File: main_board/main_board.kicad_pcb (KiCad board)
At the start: 4 copper layers, 85 x 55 mm, 58 parts, among them J1 USB4105-GF-A-060, J2 Conn_ARM_JTAG_SWD_10, Q3 NX3008PBK,215, U1 SSD1306, U2 ESP32-S2-SOLO, U3 TLV62568PDRLT, U4 MCP73832, U5 DW01, U6 8205A, U7 MAX17055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

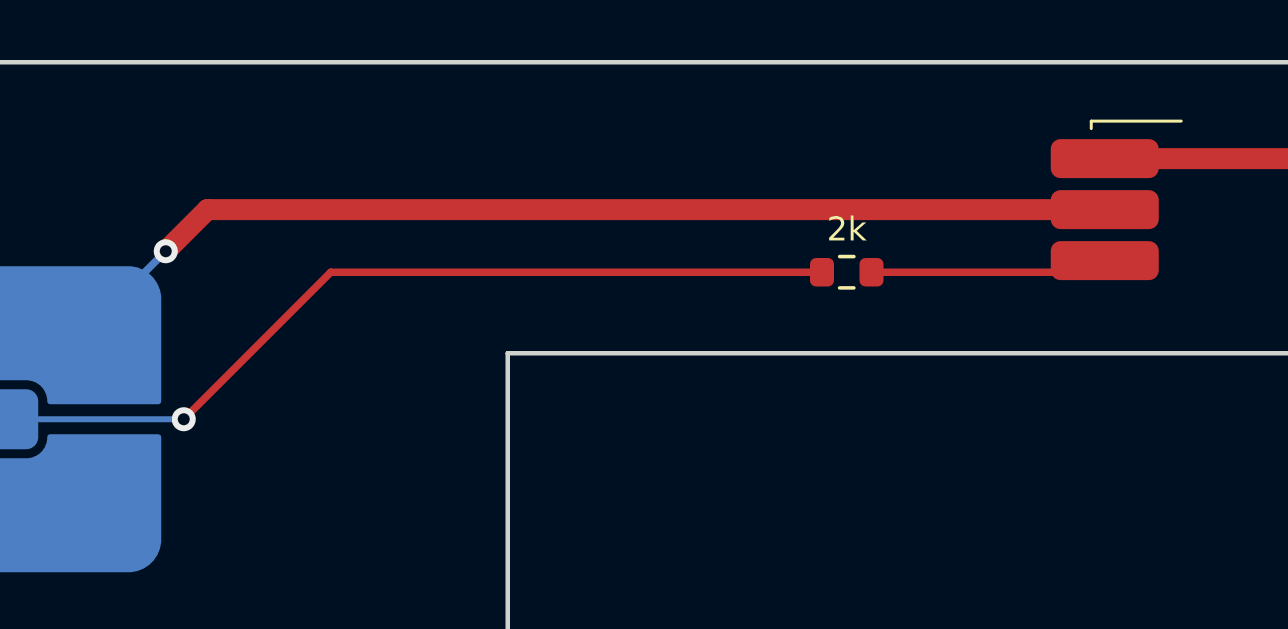
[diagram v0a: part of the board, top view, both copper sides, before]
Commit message: Tweak touch detector circuit
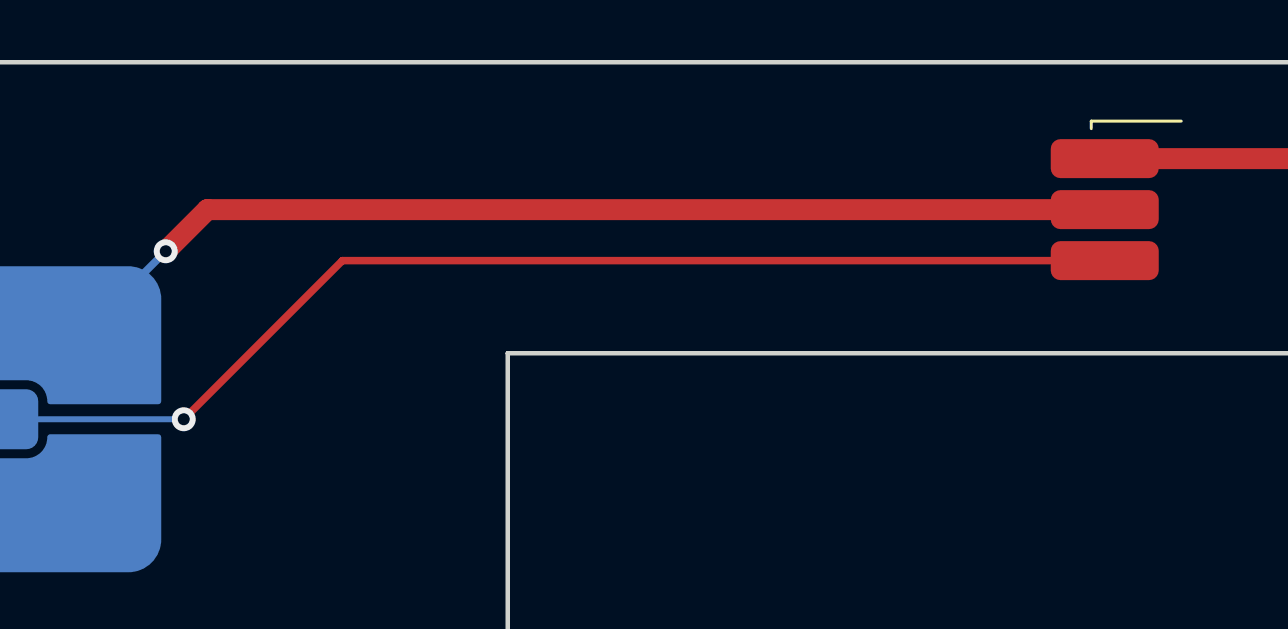
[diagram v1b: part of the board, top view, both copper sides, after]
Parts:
- removed R17: 2k, Resistor_SMD:R_0603_1608Metric
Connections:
- E2 pad 1: Net-(E2-Pad1) -> Net-(M1-RLD_OUT)
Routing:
- net Net-(M1-RLD_OUT): track 7.39 -> 38.7 mm, vias 0 -> 1
- net Net-(E2-Pad1): track 29.2 -> 0.00 mm, vias 1 -> 0

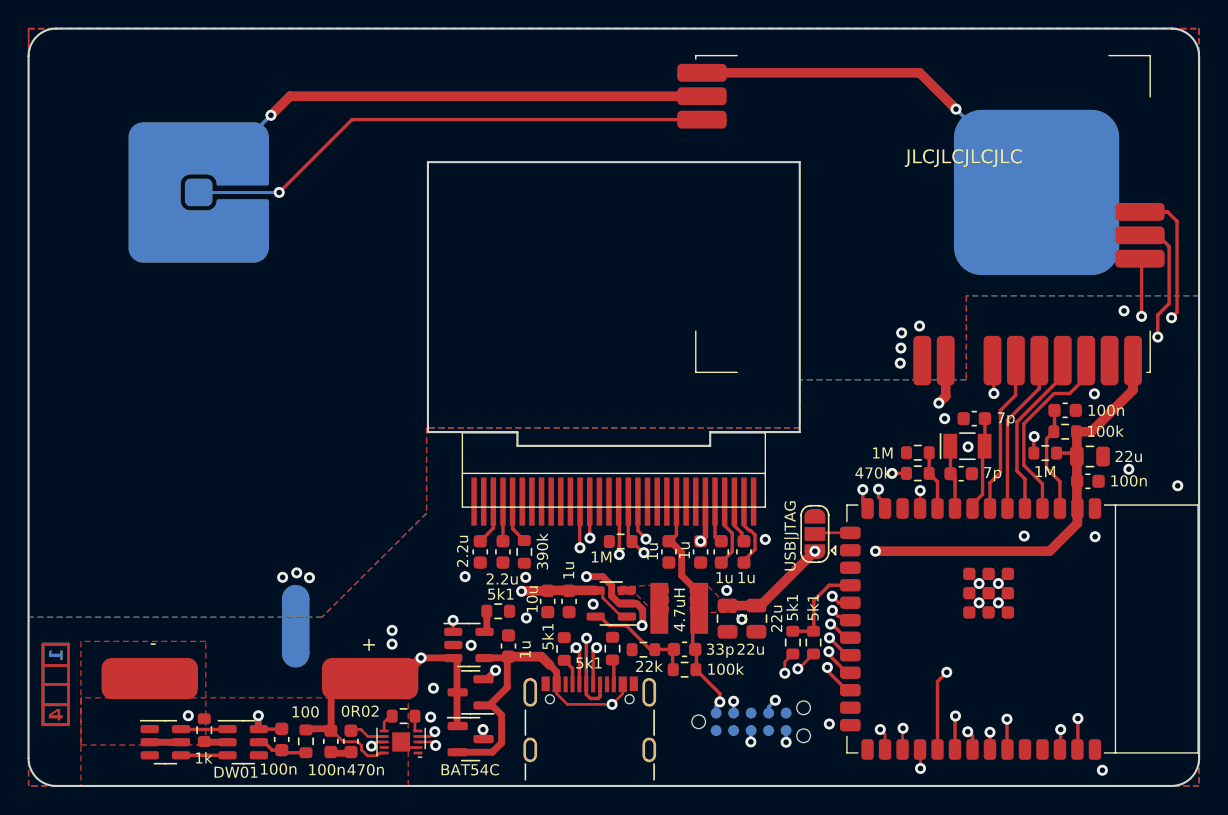
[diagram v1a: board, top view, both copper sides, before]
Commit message: Shrink frontend a bit
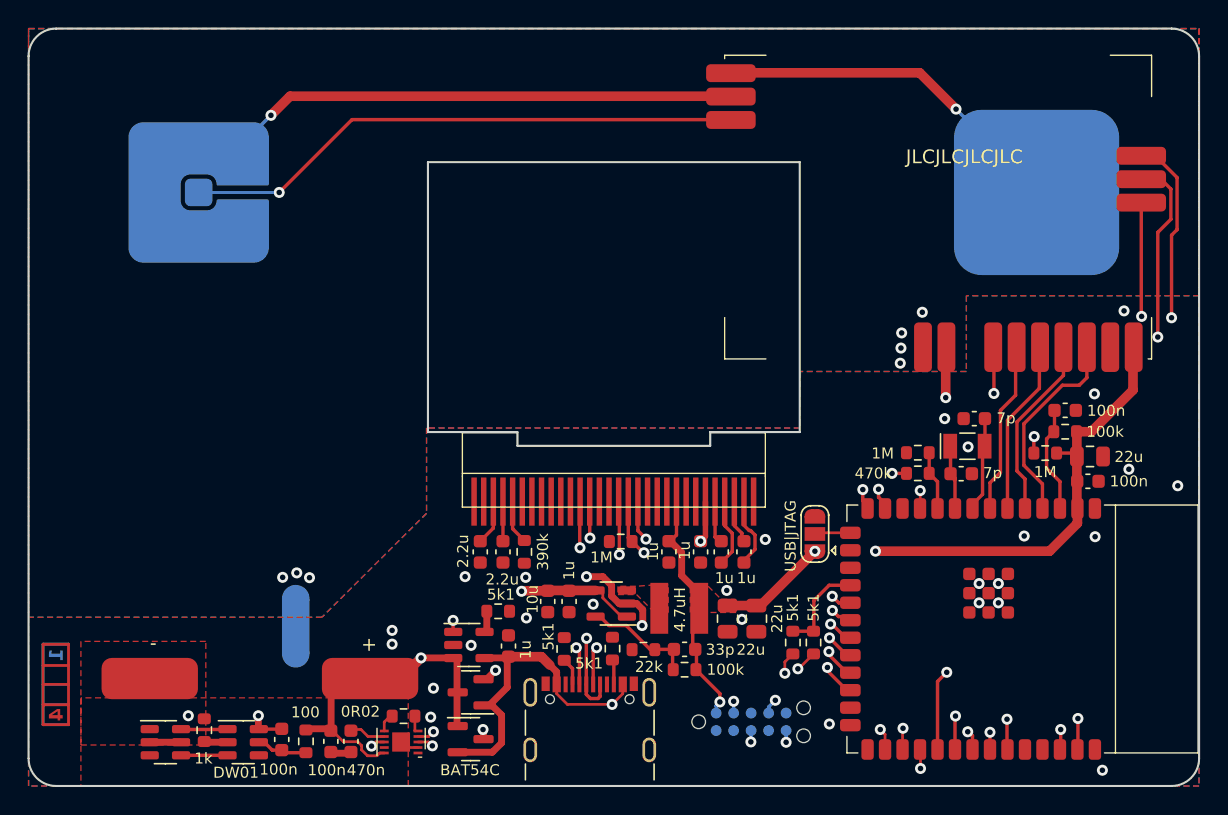
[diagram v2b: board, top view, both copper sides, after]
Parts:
- moved M1 2.32 mm to (130.8, 68.7)
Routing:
- net /ECG_CLK_EN: track 42.2 -> 46.4 mm
- net /ECG_EN: track 41.4 -> 45.5 mm
- net /~{TOUCH}: track 44.9 -> 47.4 mm
- net Net-(M1-~{DRDY}): track 13.1 -> 15.4 mm
- net Net-(M1-ECG_L): track 23.0 -> 20.9 mm
- net /BATT_SCL: track 43.3 -> 41.2 mm
- net Net-(M1-MISO): track 11.7 -> 13.9 mm
- net /BATT_SDA: track 45.5 -> 43.4 mm
- net Net-(M1-RLD_OUT): track 38.7 -> 40.8 mm
- net Net-(M1-ECG_R): track 34.7 -> 36.8 mm

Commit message: Fix rule violation, use a single plane on front side
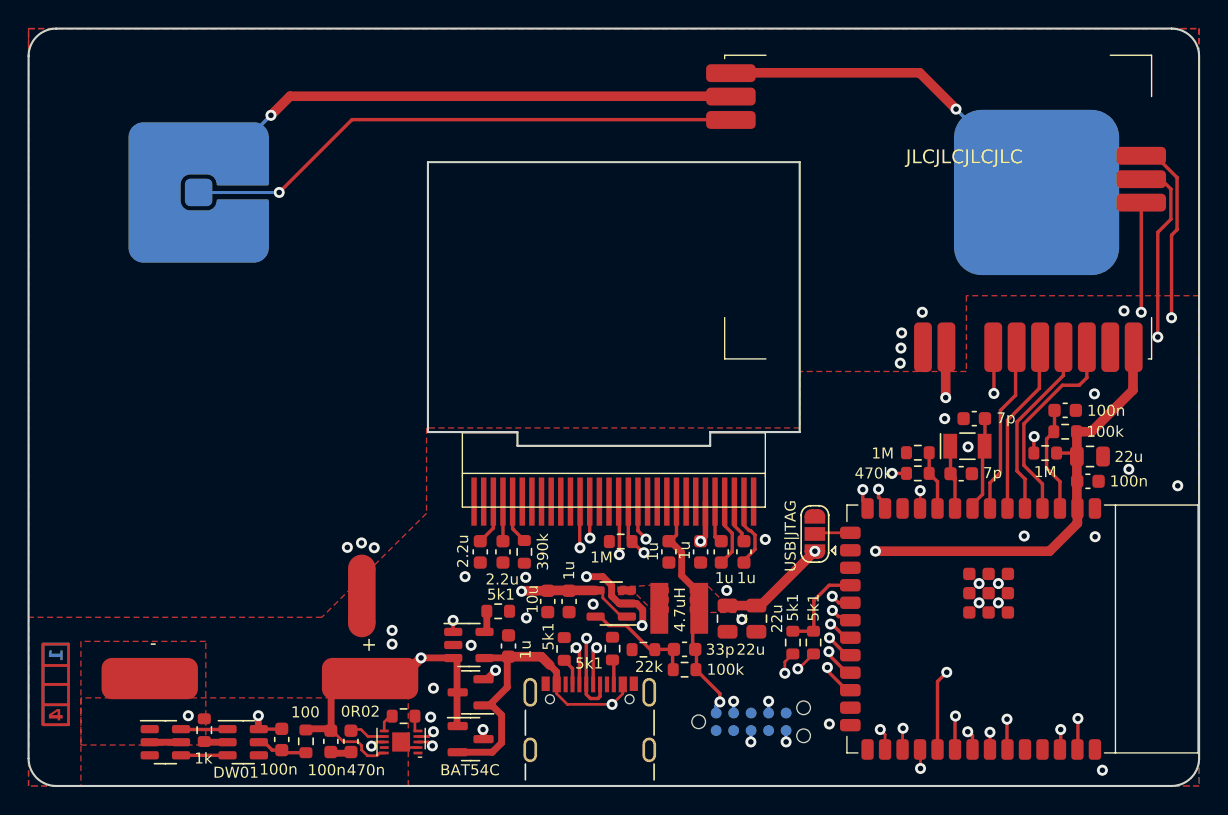
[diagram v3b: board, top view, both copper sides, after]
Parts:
- NT1: moved to F.Cu
- moved NT1 5.28 mm to (104.2, 86.2)
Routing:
- removed copper zone on B.Cu, net GNDA

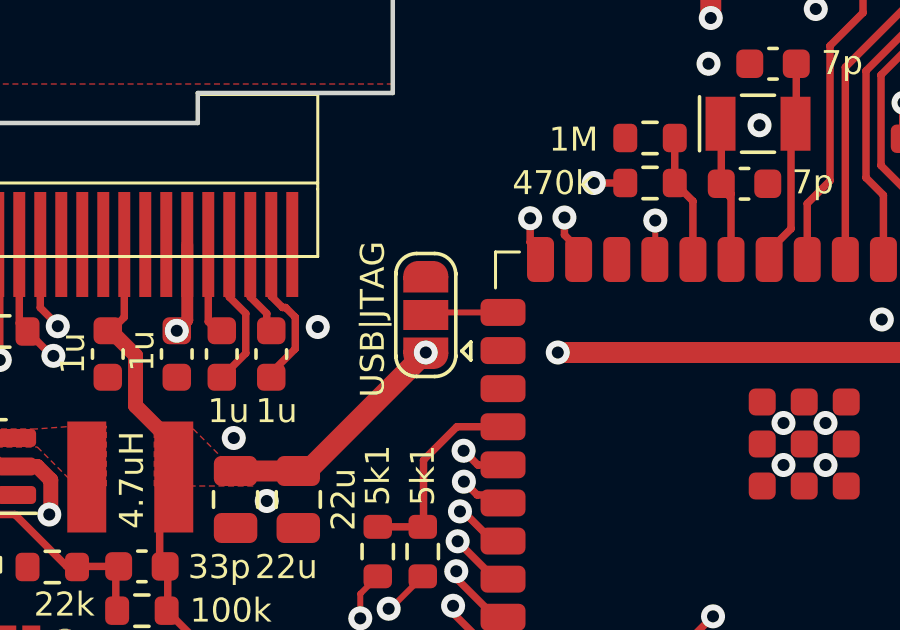
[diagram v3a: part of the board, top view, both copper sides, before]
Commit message: Remove JTAG selector
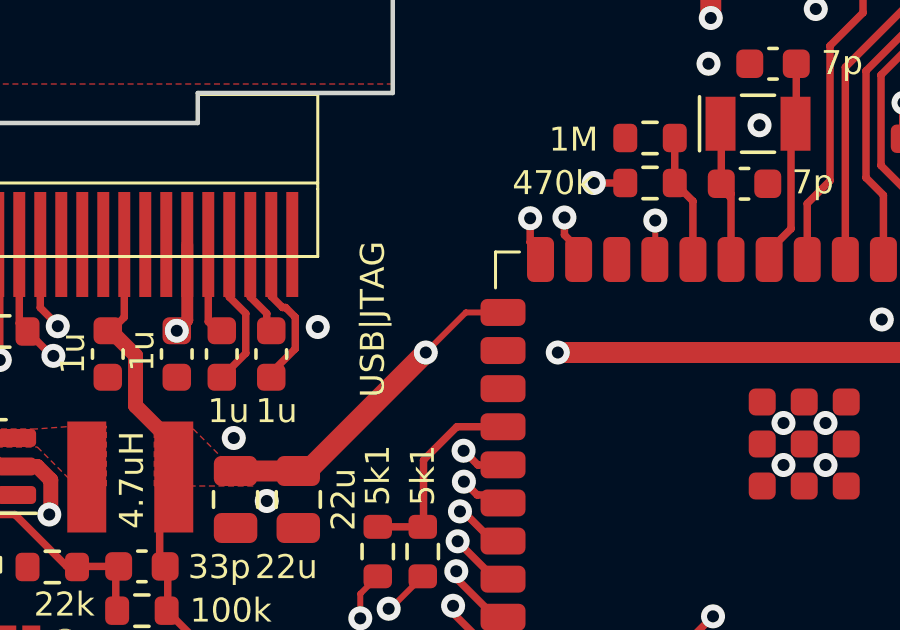
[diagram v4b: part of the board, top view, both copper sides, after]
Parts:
- removed JP1: SolderJumper_3_Open, Jumper:SolderJumper-3_P1.3mm_Open_RoundedPad1.0x1.5mm
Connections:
- U2 pad 15: Net-(JP1-C) -> +3V3
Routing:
- net +3V3: track 57.6 -> 60.8 mm
- net Net-(JP1-C): track 2.54 -> 0.00 mm

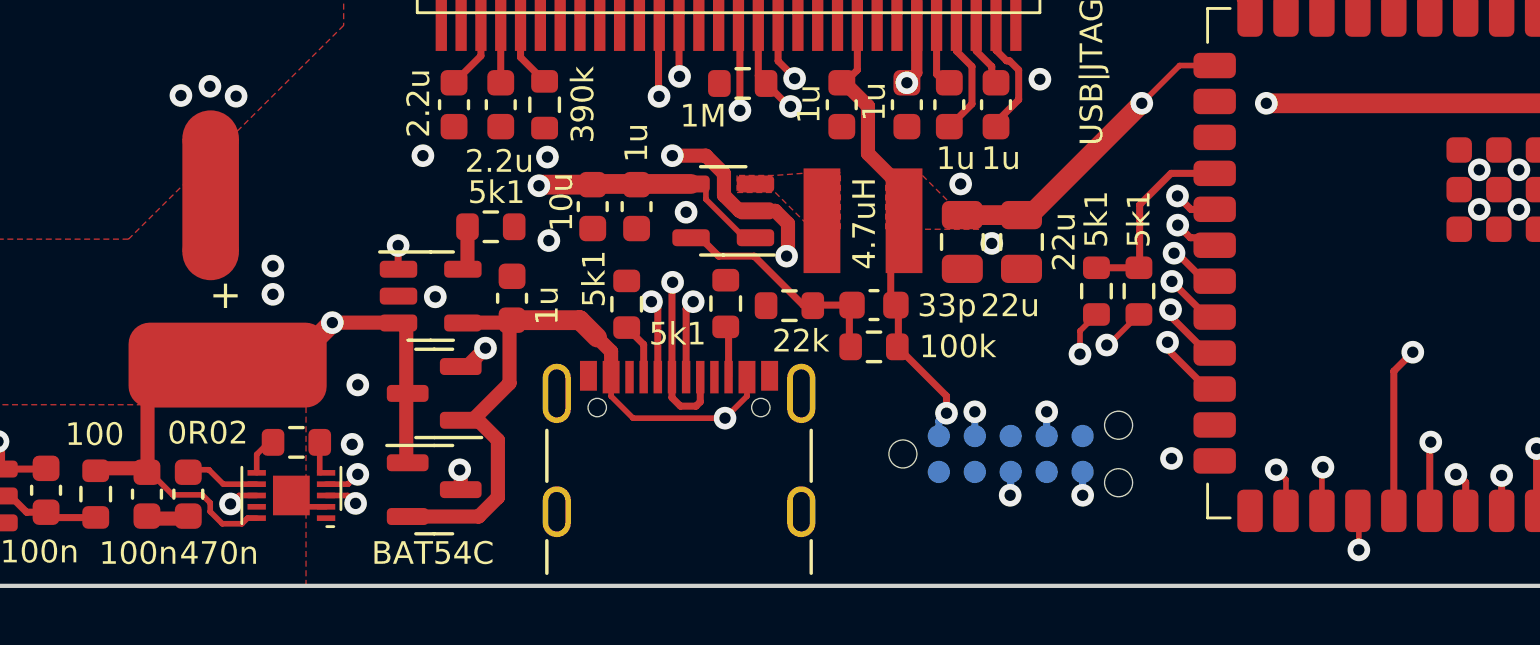
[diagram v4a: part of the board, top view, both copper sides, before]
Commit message: Replace battery alert input with ADC_EN
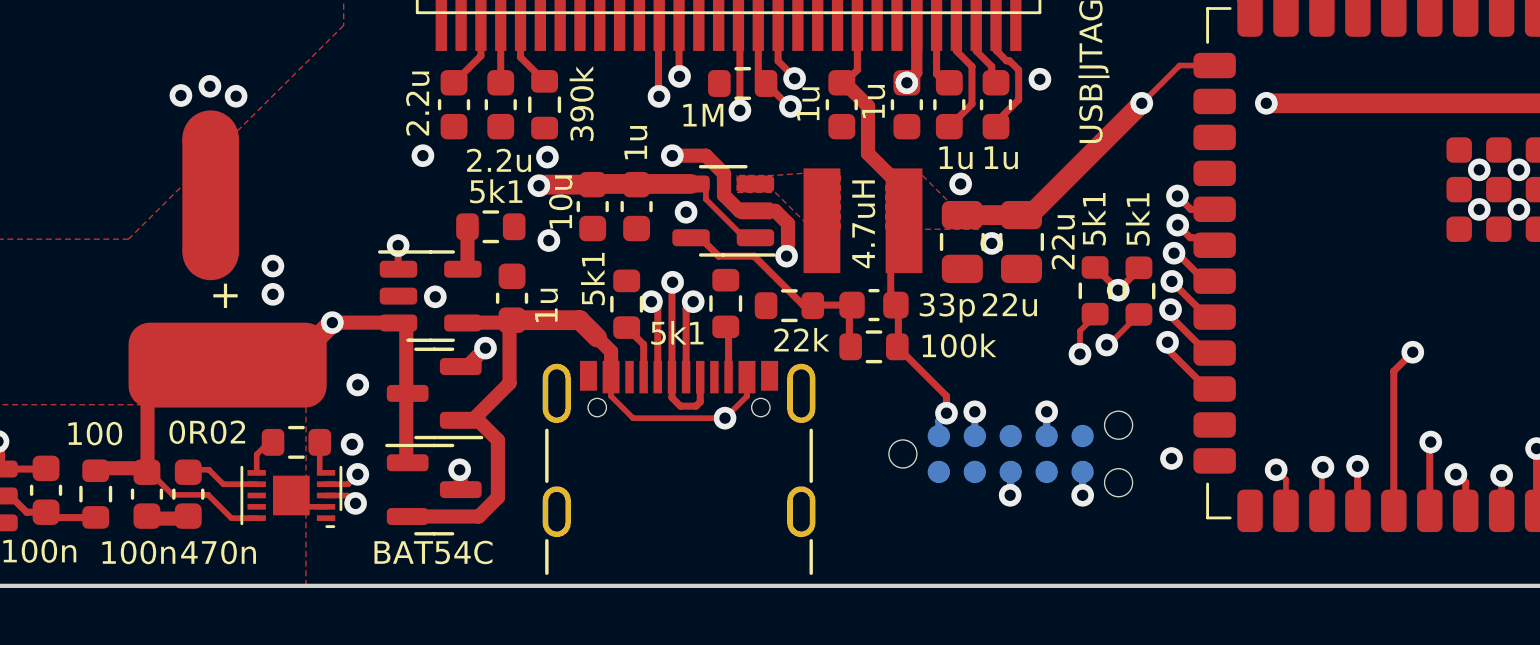
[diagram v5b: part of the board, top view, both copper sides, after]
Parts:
- moved R9 0.05 mm to (135.4, 89.6)
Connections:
- U2 pad 18: /ADC_EN -> unconnected-(U2-IO10-Pad18)
- U2 pad 30: /BATT_ALERT -> /ADC_EN
- U7 pad 8: /BATT_ALERT -> unconnected-(U7-~{ALERT}-Pad8)
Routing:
- net /BATT_ALERT: track 42.5 -> 0.00 mm, vias 2 -> 0
- net /ADC_EN: track 6.87 -> 15.5 mm, vias 0 -> 2
- net /CHG_STAT: track 34.9 -> 35.6 mm

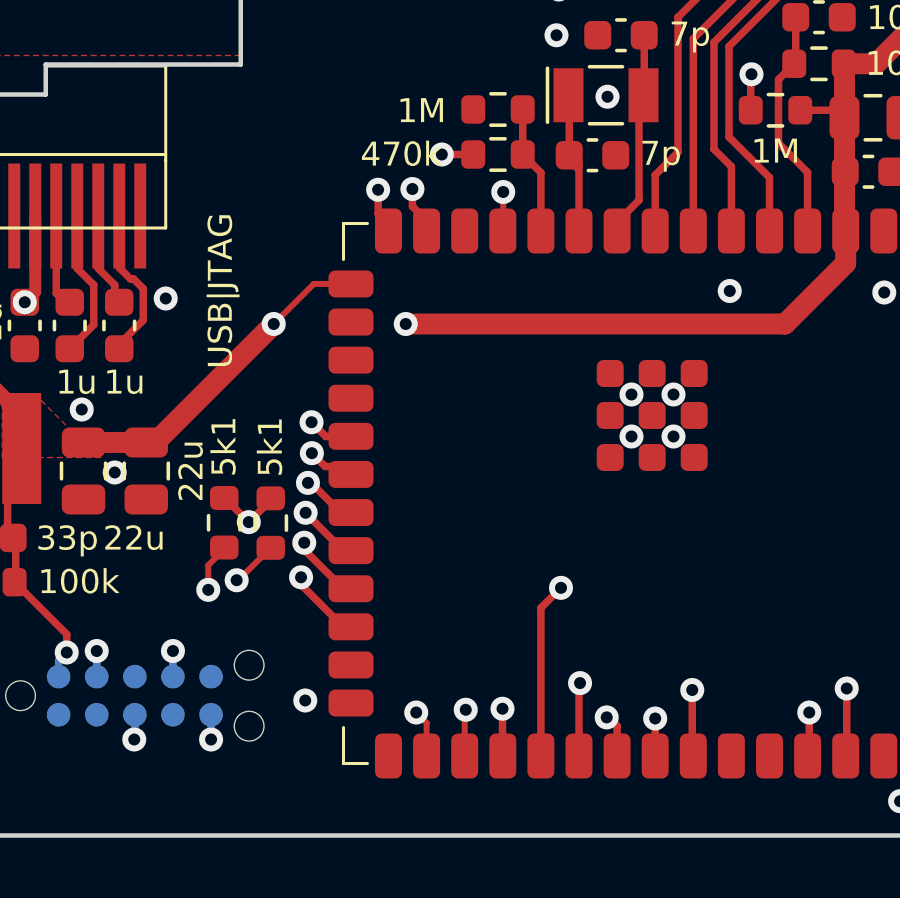
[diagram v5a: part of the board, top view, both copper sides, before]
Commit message: Move frontend chip select to IO0
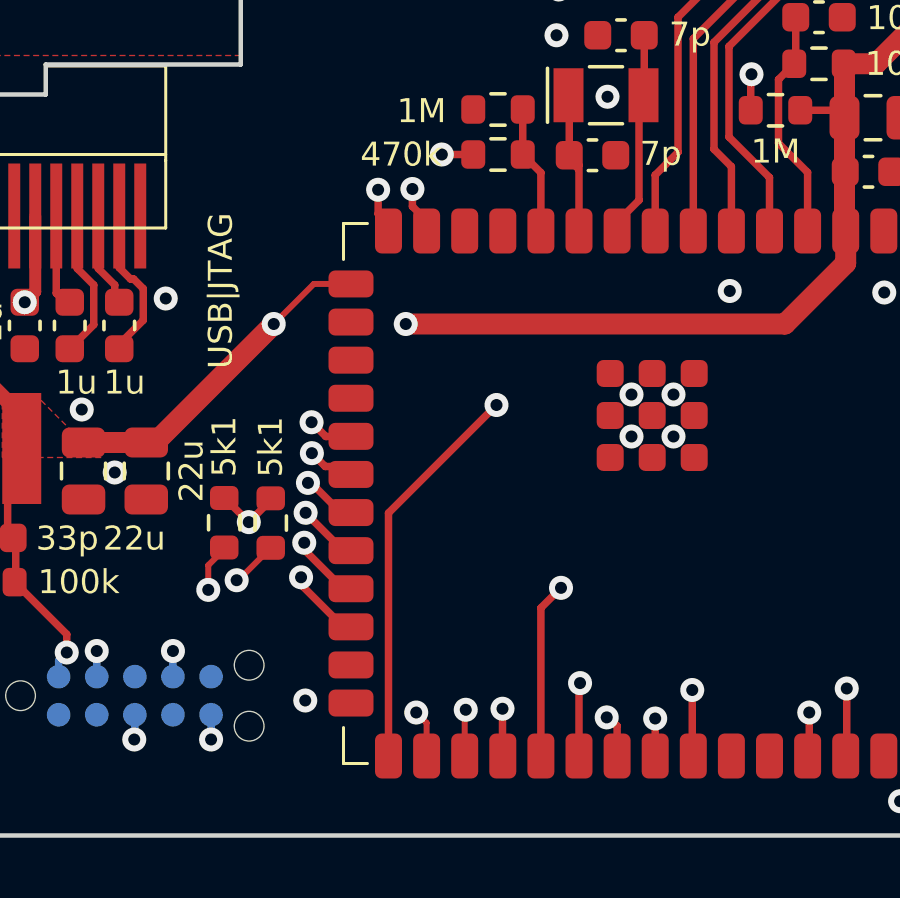
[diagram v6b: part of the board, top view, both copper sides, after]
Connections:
- M1 pad 6: Net-(M1-~{CS}) -> /ECG_CS
- R3 pad 2: Net-(M1-~{CS}) -> /ECG_CS
- U2 pad 11: Net-(M1-~{CS}) -> unconnected-(U2-IO18-Pad11)
- U2 pad 27: unconnected-(U2-IO0-Pad27) -> /ECG_CS
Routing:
- net /ECG_CS: track 0.00 -> 35.9 mm, vias 0 -> 3
- net Net-(M1-~{CS}): track 17.9 -> 0.00 mm, vias 3 -> 0

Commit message: Merge ECG_EN and ADC_EN
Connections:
- M1 pad 14: /ECG_EN -> /ANALOG_EN
- R11 pad 1: /ADC_EN -> /ANALOG_EN
- R9 pad 1: /ADC_EN -> /ANALOG_EN
- U2 pad 11: unconnected-(U2-IO18-Pad11) -> /~{DISPLAY_RES}
- U2 pad 12: unconnected-(U2-IO8-Pad12) -> /~{DISPLAY_CS}
- U2 pad 19: /~{DISPLAY_CS} -> unconnected-(U2-IO11-Pad19)
- U2 pad 20: /~{DISPLAY_RES} -> unconnected-(U2-IO12-Pad20)
- U2 pad 30: /ADC_EN -> unconnected-(U2-IO37-Pad30)
- U2 pad 38: /ECG_EN -> /ANALOG_EN
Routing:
- net /ANALOG_EN: track 0.00 -> 68.5 mm, vias 0 -> 3
- net /ECG_EN: track 45.5 -> 0.00 mm, vias 2 -> 0
- net /ADC_EN: track 15.5 -> 0.00 mm, vias 2 -> 0
- net /~{DISPLAY_RES}: track 20.6 -> 26.6 mm
- net /~{DISPLAY_CS}: track 19.7 -> 23.9 mm
- net /ECG_CLK_EN: track 46.4 -> 48.2 mm
